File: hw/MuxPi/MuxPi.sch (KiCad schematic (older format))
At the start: 2 parts

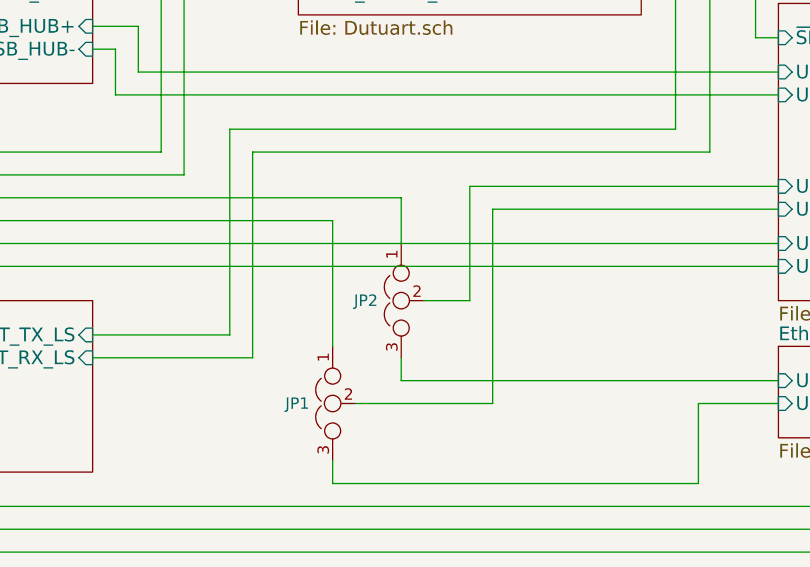
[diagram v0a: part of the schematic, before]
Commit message: Add detailed info to MuxPi electronic components
The additional information includes manufacturer names and
manufacturer symbols for all components except ceramic capacitors
and resistors. It allows to create BOM (Bill Of Materials) with
actual product names.

Change-Id: Id1c518bba60322d4b8b132ad14261806070abc27
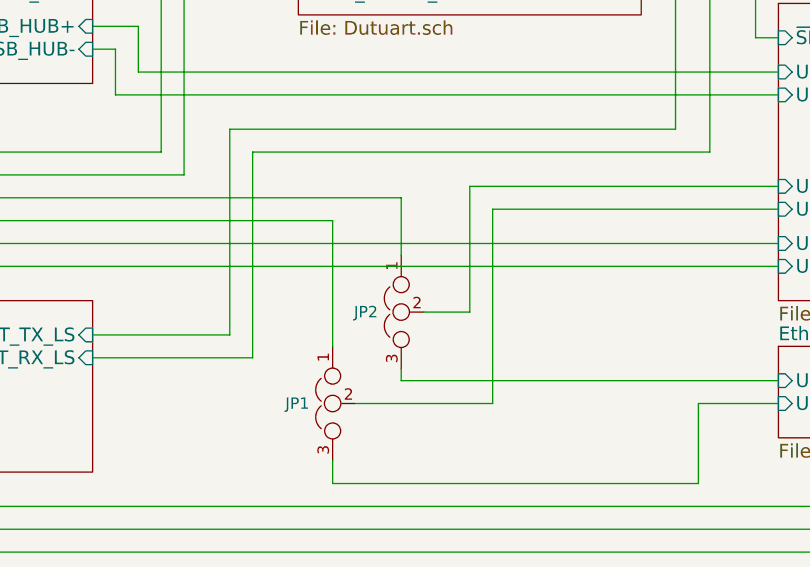
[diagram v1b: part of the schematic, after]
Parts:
- JP1, JP2: Manufacturer (none) -> CONNFLY; Symbol (none) -> DS1021-1*3SF1-1
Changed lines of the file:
@@
 	6300 4800 4950 4800
 Wire Wire Line
-	4950 4800 4950 5300
+	4950 4800 4950 5350
 Wire Wire Line
-	4950 5300 4750 5300
+	4950 5350 4750 5350
 Wire Wire Line
-	4650 5550 4650 5650
+	4650 5600 4650 5650
 Wire Wire Line
 	4650 5650 6300 5650
-Wire Wire Line
-	4650 5050 4650 4850
 Wire Wire Line
 	4650 4850 1200 4850
@@
 F 3 "http://www.tme.eu/pl/Document/cc301e58a5da78cb543a94b5a5b7f06a/DS1021.pdf" H 4350 5750 50  0001 C CNN
 F 4 "http://www.tme.eu/pl/details/zl201-03g/listwy-i-gniazda-kolkowe/connfly/ds1021-1_3sf1-1/" V 4350 5750 60  0001 C CNN "Shop link"
+F 5 "CONNFLY" V 4350 5750 50  0001 C CNN "Manufacturer"
+F 6 "DS1021-1*3SF1-1" V 4350 5750 50  0001 C CNN "Symbol"
 	1    4350 5750
 	0    -1   1    0
@@
 Wire Wire Line
 	5950 5750 6300 5750
-$Comp
-L MuxPi:Jumper_NC_Dual JP2
-U 1 1 584EA671
-P 4650 5300
-F 0 "JP2" V 4650 5402 50  0000 L CNN
-F 1 "DS1021-1*3SF1-1" V 4695 5402 50  0001 L CNN
-F 2 "Socket_Strips:Socket_Strip_Straight_1x03" H 4650 5300 50  0001 C CNN
-F 3 "http://www.tme.eu/pl/Document/cc301e58a5da78cb543a94b5a5b7f06a/DS1021.pdf" H 4650 5300 50  0001 C CNN
-F 4 "http://www.tme.eu/pl/details/zl201-03g/listwy-i-gniazda-kolkowe/connfly/ds1021-1_3sf1-1/" V 4650 5300 60  0001 C CNN "Shop link"
-	1    4650 5300
-	0    -1   1    0
-$EndComp
 Wire Wire Line
 	8800 2200 9000 2200
@@
 Wire Wire Line
 	3600 2800 6300 2800
+Wire Wire Line
+	4650 4850 4650 5100
+$Comp
+L MuxPi:Jumper_NC_Dual JP2
+U 1 1 5A8A431E
+P 4650 5350
+F 0 "JP2" V 4650 5452 50  0000 L CNN
+F 1 "DS1021-1*3SF1-1" V 4695 5452 50  0001 L CNN
+F 2 "Socket_Strips:Socket_Strip_Straight_1x03" H 4650 5350 50  0001 C CNN
+F 3 "http://www.tme.eu/pl/Document/cc301e58a5da78cb543a94b5a5b7f06a/DS1021.pdf" H 4650 5350 50  0001 C CNN
+F 4 "http://www.tme.eu/pl/details/zl201-03g/listwy-i-gniazda-kolkowe/connfly/ds1021-1_3sf1-1/" V 4650 5350 60  0001 C CNN "Shop link"
+F 5 "CONNFLY" V 4650 5350 50  0001 C CNN "Manufacturer"
+F 6 "DS1021-1*3SF1-1" V 4650 5350 50  0001 C CNN "Symbol"
+	1    4650 5350
+	0    -1   1    0
+$EndComp
 $EndSCHEMATC

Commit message: Update  hardware design to version 1.4
Change-Id: I72a4381d8bec5616bc1cfe04dc8a5407141c77d5
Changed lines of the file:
@@
 EESchema Schematic File Version 4
 LIBS:MuxPi-cache
-EELAYER 26 0
+EELAYER 29 0
 EELAYER END
 $Descr A4 11693 8268
@@
 Sheet 1 12
 Title "MuxPi"
-Date "2018-08-14"
-Rev "1.3"
+Date "2018-11-16"
+Rev "1.4"
 Comp "SRPOL"
 Comment1 "Author: Adam Malinowski <a.malinowsk2@partner.samsung.com>"
@@
 F20 "WD_RESET" I L 1500 2050 60
 F21 "PI_GPIO_1" I R 3300 3150 60
+F22 "USB_DUT-" I L 1500 3400 60
+F23 "USB_DUT+" I L 1500 3300 60
 $EndSheet
 $Sheet
@@
 	3300 2550 6300 2550
 Wire Wire Line
-	3300 2700 3700 2700
-Wire Wire Line
-	3300 2800 3600 2800
-Wire Wire Line
 	3300 2950 6300 2950
 Wire Wire Line
@@
 F5 "LTHOR_ID" I L 1500 5850 60
 F6 "LTHOR_SWITCH" I L 1500 5950 60
-F7 "ADC2" I L 1500 5500 60
-F8 "ADC1" I L 1500 5400 60
+F7 "USB_LTHOR-" I L 1500 5550 60
+F8 "USB_LTHOR+" I L 1500 5450 60
 $EndSheet
 Wire Wire Line
@@
 Wire Wire Line
 	6000 3750 5700 3750
-Wire Wire Line
-	1500 5400 1400 5400
-Wire Wire Line
-	1400 5400 1400 4750
-Wire Wire Line
-	1400 4750 3700 4750
-Wire Wire Line
-	3700 4750 3700 2700
-Connection ~ 3700 2700
-Wire Wire Line
-	1500 5500 1300 5500
-Wire Wire Line
-	1300 5500 1300 4650
-Wire Wire Line
-	1300 4650 3600 4650
-Wire Wire Line
-	3600 4650 3600 2800
-Connection ~ 3600 2800
-Wire Wire Line
-	3700 2700 6300 2700
-Wire Wire Line
-	3600 2800 6300 2800
 Wire Wire Line
 	4650 4850 4650 5100
@@
 	0    -1   1    0
 $EndComp
+Wire Wire Line
+	3300 2700 6300 2700
+Wire Wire Line
+	3300 2800 6300 2800
+Wire Wire Line
+	1500 3400 700  3400
+Wire Wire Line
+	700  3400 700  5550
+Wire Wire Line
+	700  5550 1500 5550
+Wire Wire Line
+	1500 5450 800  5450
+Wire Wire Line
+	800  5450 800  3300
+Wire Wire Line
+	800  3300 1500 3300
 $EndSCHEMATC
